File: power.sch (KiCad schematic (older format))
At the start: 22 parts, among them J4 USB_C_Receptacle_USB2.0, Q10 Q_PMOS_GSD, SW1 SW_SPST, U13 TP4056, U14 TPS63001DRCR

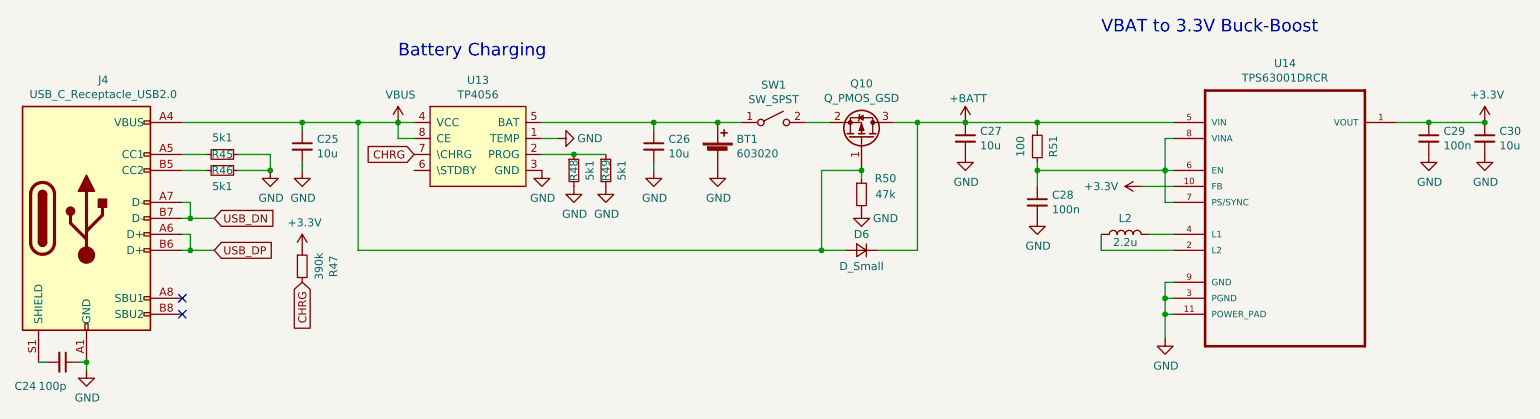
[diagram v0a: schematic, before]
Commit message: UPD: removed all p-fets, no more ideal diode
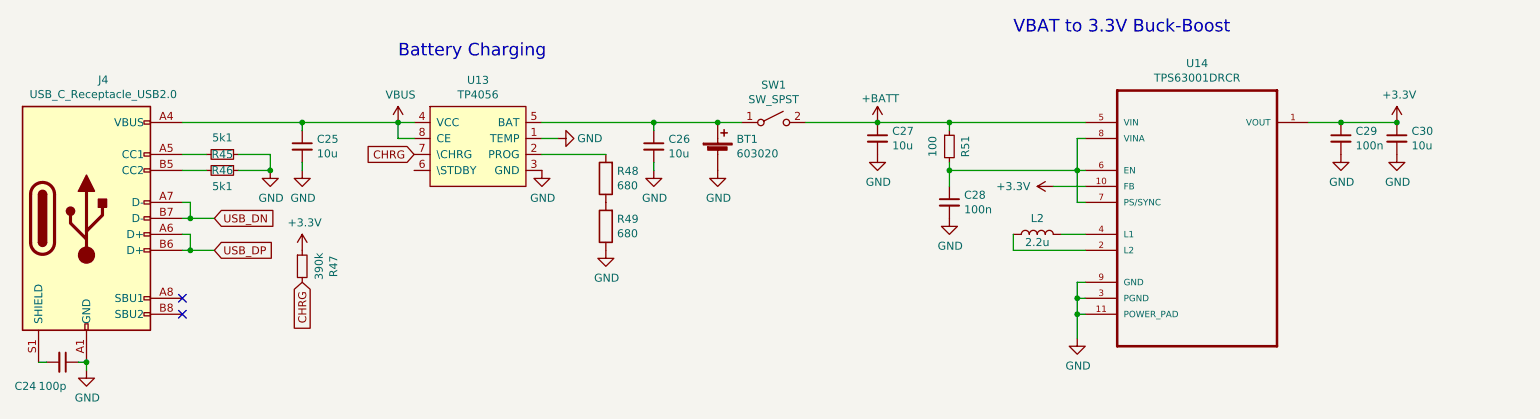
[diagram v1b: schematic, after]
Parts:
- removed D6: D_Small, Diode_SMD:D_SOD-123F, symbol Device:D_Small
- removed Q10: Q_PMOS_GSD, Package_TO_SOT_SMD:SOT-23, symbol Device:Q_PMOS_GSD
- removed R48, R49: 5k1, Resistor_SMD:R_0402_1005Metric, symbol Device:R_Small
- removed R50: 47k, Resistor_SMD:R_0402_1005Metric, symbol Device:R_Small
- added R48, R49: 680, Resistor_SMD:R_0402_1005Metric, symbol Device:R
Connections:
- net +BATT: now also SW1.2 (B)
- net GND: now also R49.1
- net at U13.2 (PROG): now also R48.2
- new net: R48.1, R49.2
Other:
- moved on the sheet: C27, C28, C29, C30, L2, R51, U14

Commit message: Finished layout
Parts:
- removed C24: 100p, Capacitor_SMD:C_0402_1005Metric, symbol Device:C_Small
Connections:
- net GND: now also J4.S1 (SHIELD)
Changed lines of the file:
@@
-$Comp
-L Device:C_Small C?
-U 1 1 5C7642B0
-P 1400 4250
-AR Path="/5C7642B0" Ref="C?"  Part="1"
-AR Path="/5C753B69/5C7642B0" Ref="C24"  Part="1"
-F 0 "C24" V 1550 3950 50  0000 L CNN
-F 1 "100p" V 1550 4100 50  0000 L CNN
-F 2 "Capacitor_SMD:C_0402_1005Metric" H 1400 4250 50  0001 C CNN
-F 3 "~" H 1400 4250 50  0001 C CNN
-	1    1400 4250
-	0    1    1    0
-$EndComp
 $Comp
 L Device:C_Small C?
@@
 	1    0    0    -1
 $EndComp
-Wire Wire Line
-	1300 4250 1250 4250
-Wire Wire Line
-	1500 4250 1550 4250
 Connection ~ 1550 4250
 Wire Wire Line
@@
 Wire Wire Line
 	6500 2750 6050 2750
+Wire Wire Line
+	1250 4250 1550 4250
 $EndSCHEMATC
